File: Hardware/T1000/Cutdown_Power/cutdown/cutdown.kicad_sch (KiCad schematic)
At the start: 34 parts, among them J2 Conn_01x06_Socket, J3 Conn_01x01_Pin, J4 Conn_01x01_Pin, Q1 NMOS, Q2 NMOS, U1 LTC1751, U2 LTC7061IMSE-WTRPBF

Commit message: V0.1 of cutdown board to add opamp scaling on current sense
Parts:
- added R8: 1.4k, Resistor_SMD:R_0603_1608Metric_Pad0.98x0.95mm_HandSolder, symbol Device:R_Small
- added R9: 39.2k, Resistor_SMD:R_0603_1608Metric_Pad0.98x0.95mm_HandSolder, symbol Device:R_Small
- added TP5, TP6: TestPoint, TestPoint:TestPoint_Pad_D1.0mm, symbol Connector:TestPoint
- added U3: TLV172IDCK, Package_TO_SOT_SMD:SOT-353_SC-70-5, symbol Amplifier_Operational:TLV172IDCK
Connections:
- net +BATT: now also BT1.2 (+); no longer BT1.1 (+)
- net GND: now also BT1.1 (-), R8.2, U3.2 (V-); no longer BT1.2 (-)
- net ISNS: now also R9.2, U3.4; no longer J4.1 (Pin_1), R6.2
- net at Q2.2 (G), U2.8 (BG): now also TP6.1
- net VCC: now reaches C5.1, D1.2 (A), L2.2, R2.2, TP4.1, U2.5 (VCC), U2.6 (BGVCC)
- net VCC: now also U3.5 (V+)
- net at Q1.2 (G), U2.11 (TG): now also TP5.1
- new net: J4.1 (Pin_1), R6.2, U3.1 (+)
- new net: R8.1, R9.1, U3.3 (-)

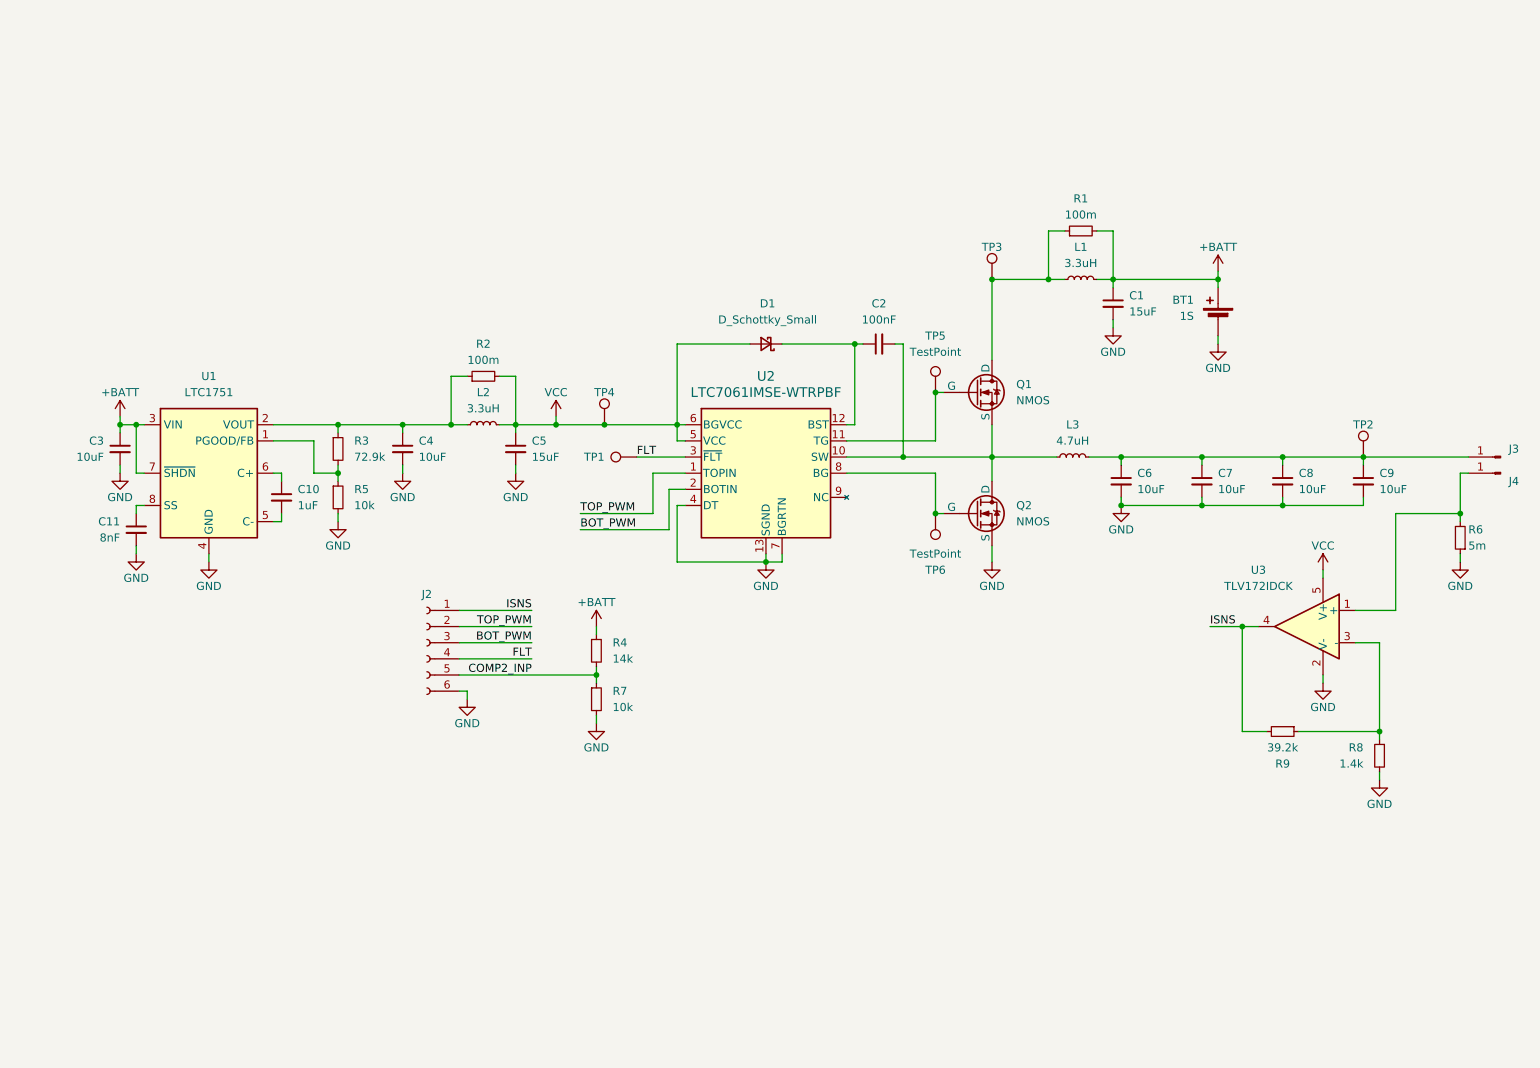
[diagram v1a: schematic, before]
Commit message: cutdown power stage V1.0 changes
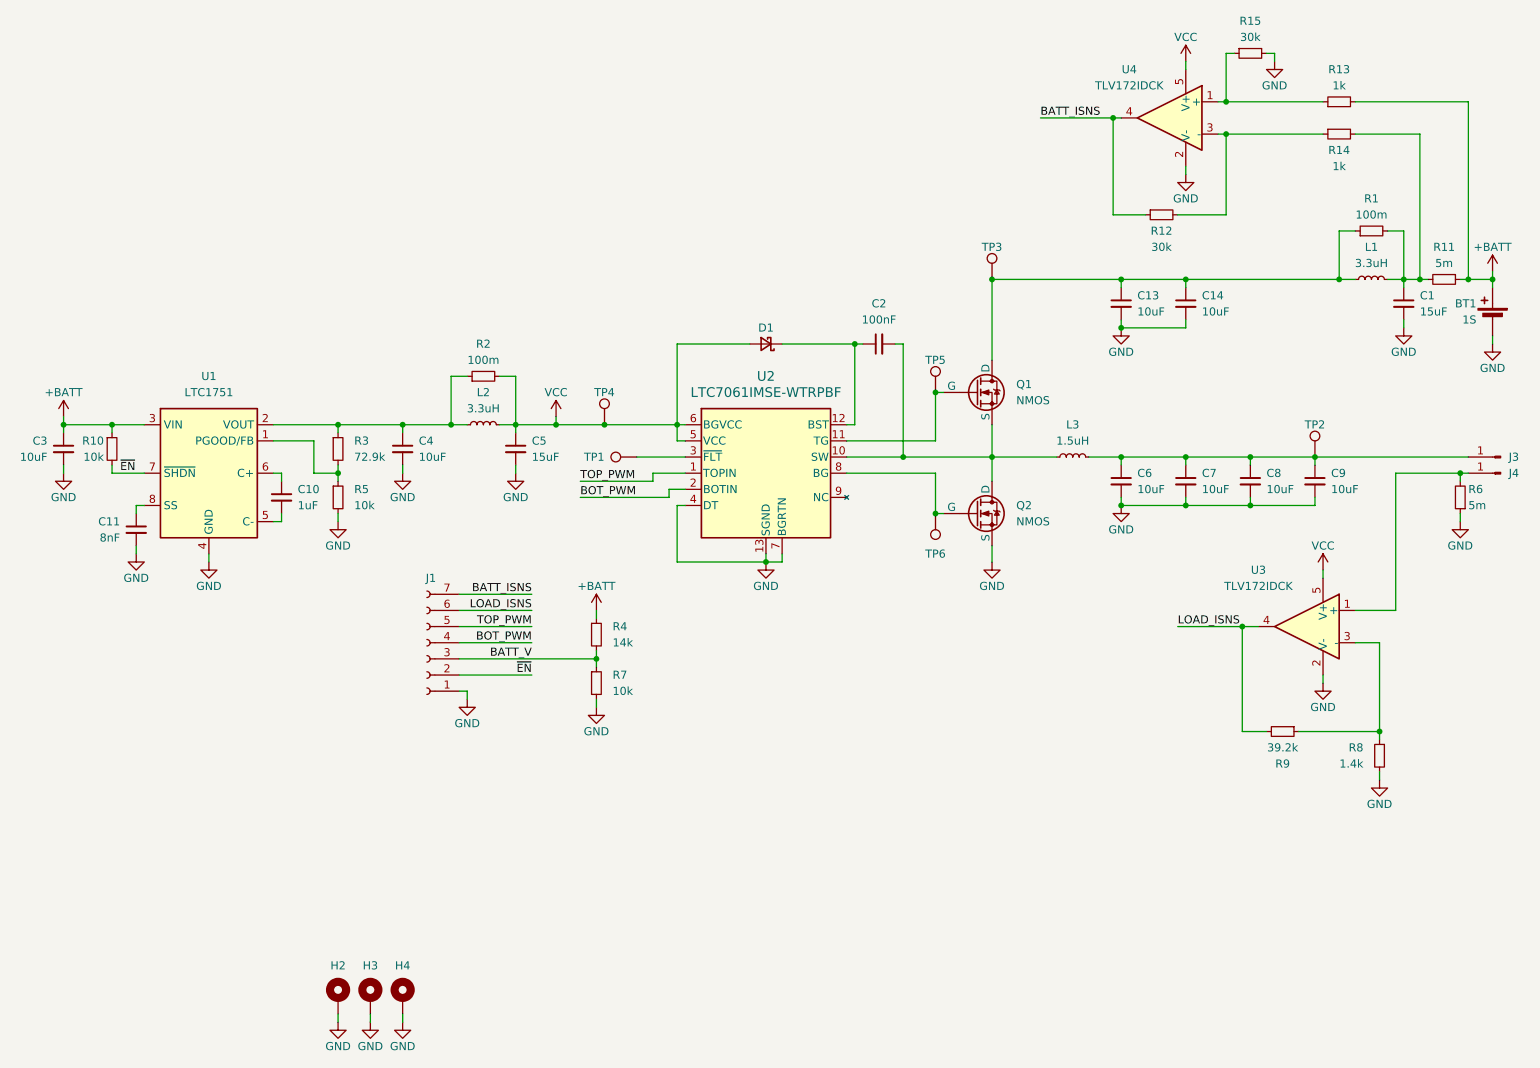
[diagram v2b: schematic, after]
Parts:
- removed J2: Conn_01x06_Socket, Connector_PinHeader_2.54mm:PinHeader_1x06_P2.54mm_Vertical, symbol Connector:Conn_01x06_Socket
- added C13, C14: 10uF, Capacitor_SMD:C_1206_3216Metric, symbol Device:C_Small
- added H2, H3, H4: MountingHole_Pad, MountingHole:MountingHole_2.2mm_M2_DIN965_Pad, symbol Mechanical:MountingHole_Pad
- added J1: Conn_01x07_Socket, BPP_Lib:Molex_ 1718570007, symbol Connector:Conn_01x07_Socket
- added R10: 10k, Resistor_SMD:R_0402_1005Metric, symbol Device:R_Small
- added R11: 5m, Resistor_SMD:R_2512_6332Metric, symbol Device:R_Small
- added R12, R15: 30k, Resistor_SMD:R_0402_1005Metric, symbol Device:R_Small
- added R13, R14: 1k, Resistor_SMD:R_0402_1005Metric, symbol Device:R_Small
- added U4: TLV172IDCK, Package_TO_SOT_SMD:SOT-353_SC-70-5, symbol Amplifier_Operational:TLV172IDCK
- L3: value 4.7uH -> 1.5uH; footprint BPP_Lib:Wurth_74437368047 -> BPP_Lib:IHLP2020CZER1R5M8A
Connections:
- net +BATT: now also R10.1, R11.1, R13.2; no longer C1.1, L1.2, R1.2, U1.7 (~{SHDN})
- net BOT_PWM: now also J1.4 (Pin_4)
- net GND: now also C13.2, C14.2, H2.1, H3.1, H4.1, J1.1 (Pin_1), R15.2, U4.2 (V-)
- net TOP_PWM: now also J1.5 (Pin_5)
- net VCC: now also U4.5 (V+)
- net at L1.1, Q1.1 (D), R1.1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: now also C13.1, C14.1
- net COMP2_INP renamed BATT_V
- net BATT_V: now also J1.3 (Pin_3)
- net FLT: no longer names the net of TP1.1, U2.3 (~{FLT})
- net ISNS renamed LOAD_ISNS
- net LOAD_ISNS: now also J1.6 (Pin_6)
- new net: C1.1, L1.2, R1.2, R11.2, R14.2
- new net: R13.1, R15.1, U4.1 (+)
- new net: R12.2, R14.1, U4.3 (-)
- new net BATT_ISNS: J1.7 (Pin_7), R12.1, U4.4
- new net ~{EN}: J1.2 (Pin_2), R10.2, U1.7 (~{SHDN})
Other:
- title: (none) -> Terminator Cutdown Power Stage
- moved on the sheet: BT1, C1, C3, C7, C8, C9, L1, R1, R4, R6, R7, TP2
